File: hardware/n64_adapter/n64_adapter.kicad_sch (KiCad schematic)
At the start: 7 parts, among them J1 N64_Slot, J2 CART SLOT TOP ROW, J3 CART SLOT BOTTOM ROW, J4 Conn_01x01, J5 Conn_01x01, J6 Conn_01x01

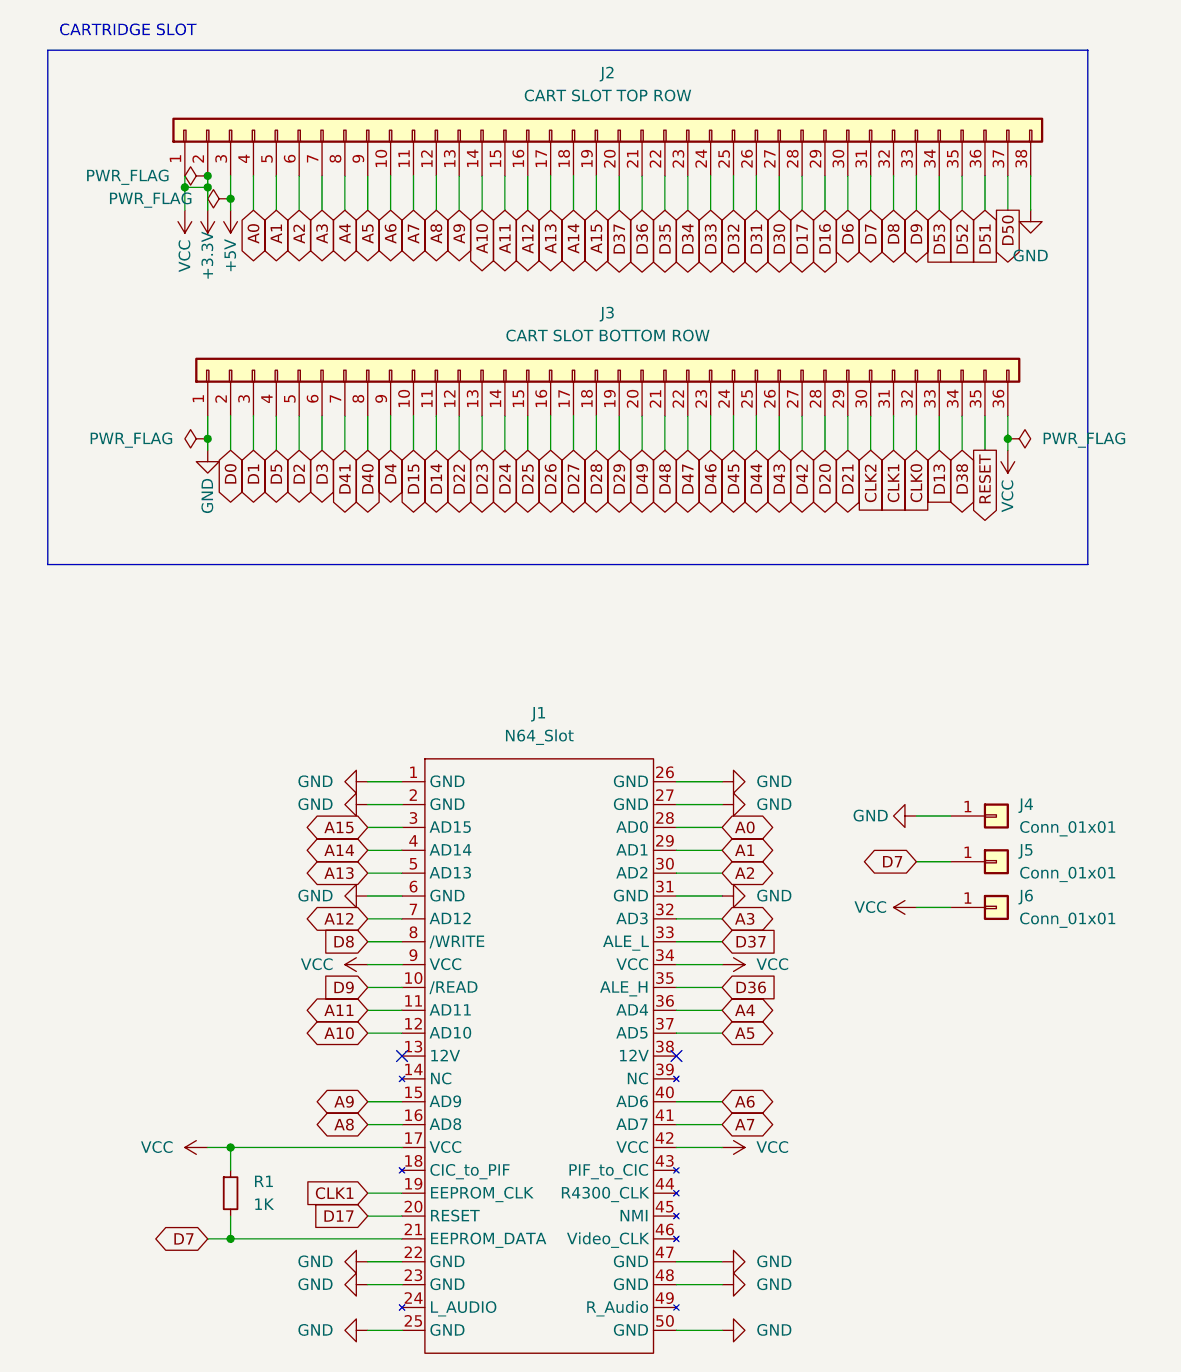
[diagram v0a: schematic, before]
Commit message: Update N64 breakout
add controller port to schematic and board. change board to inch standard, minimize trace width and reroute all traces. realign bottom silkscreen to pins.
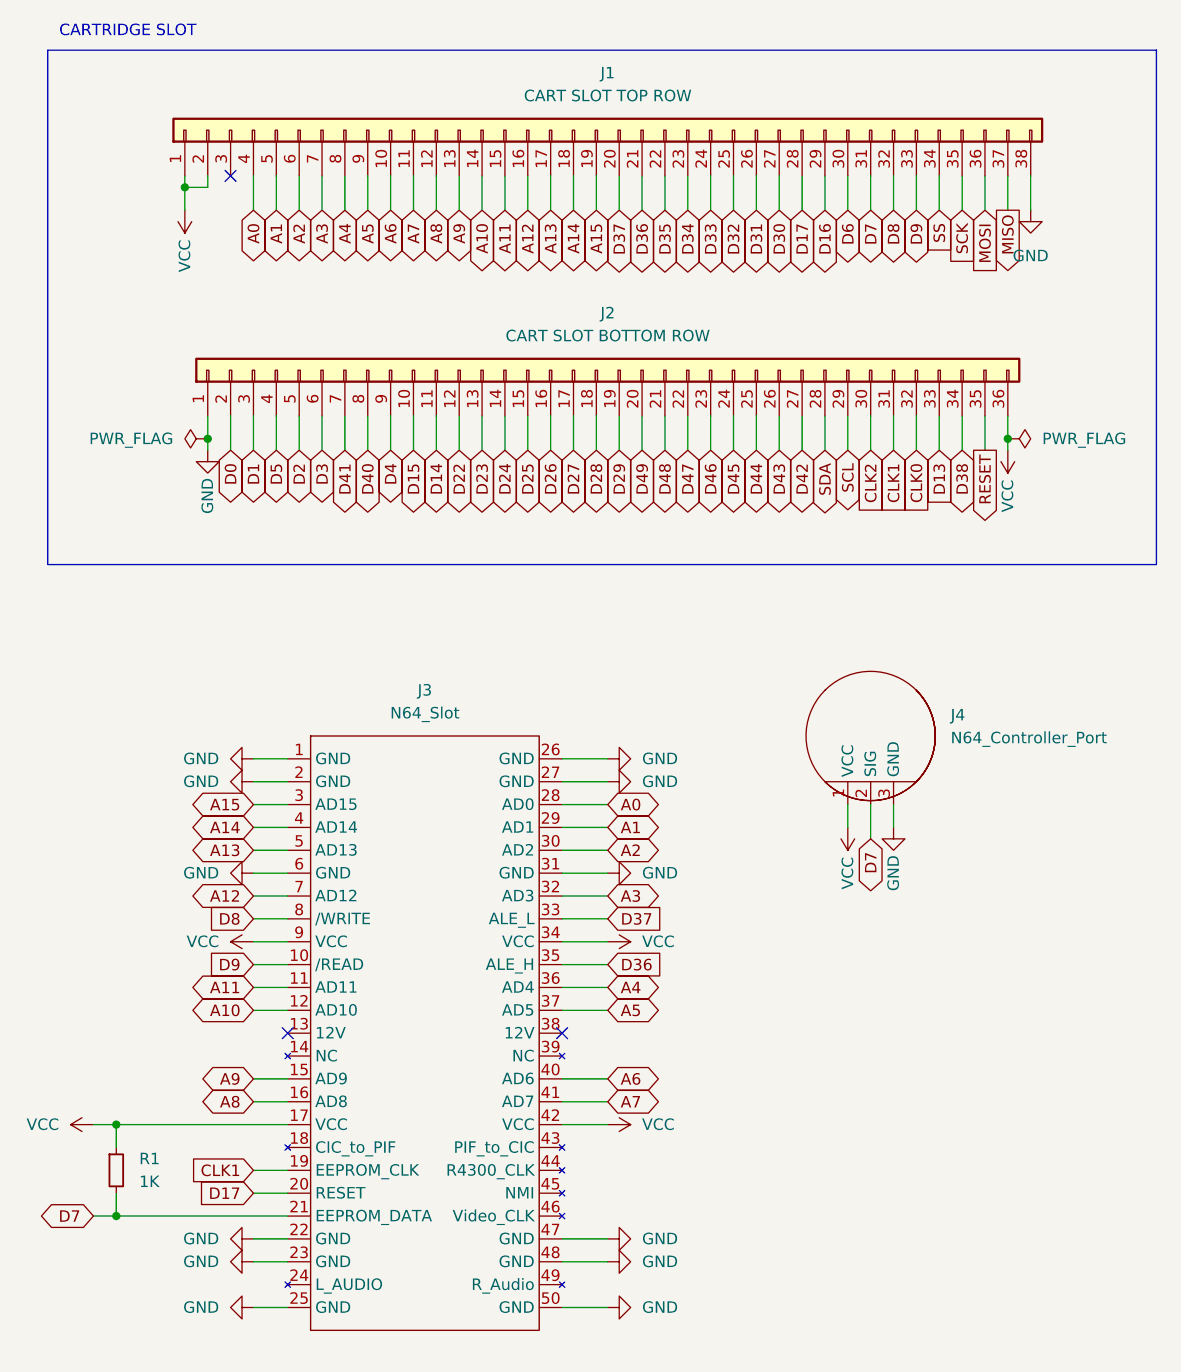
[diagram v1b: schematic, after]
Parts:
- removed J4, J5, J6: Conn_01x01, symbol Connector_Generic:Conn_01x01
- added J4: N64_Controller_Port, !OSCR:N64_CONTROLLER_PORT, symbol !OSCR:N64_Controller_Port
- J1: renamed from J2; footprint Connector_PinSocket_2.54mm:PinSocket_1x38_P2.54mm_Vertical -> Connector_PinHeader_2.54mm:PinHeader_1x38_P2.54mm_Vertical
- J2: renamed from J3; footprint Connector_PinSocket_2.54mm:PinSocket_1x36_P2.54mm_Vertical -> Connector_PinHeader_2.54mm:PinHeader_1x36_P2.54mm_Vertical
- J3: renamed from J1; footprint (none) -> !OSCR:N64 Slot; symbol sanni:N64_Slot -> !OSCR:N64_Slot
- R1: footprint (none) -> Resistor_THT:R_Axial_DIN0207_L6.3mm_D2.5mm_P10.16mm_Horizontal
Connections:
- net D7: now also J4.2 (SIG)
- net GND: now also J4.3 (GND)
- net +3V3 renamed VCC
- net VCC: now also J4.1 (VCC)
- net +5V: no longer names the net of J1.3 (Pin_3)
- net D20 renamed SDA
- net D21 renamed SCL
- net D50 renamed MISO
- net D51 renamed MOSI
- net D52 renamed SCK
- net D53 renamed SS
- no-connect marks 2 -> 3
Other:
- title: OSCR N64 ADAPTER -> OSCR N64 Breakout
- moved on the sheet: J3, R1

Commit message: finalize n64 breakout design
Ready for RTM
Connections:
- net CLK0: no longer names the net of J2.32 (Pin_32)
- net CLK2: no longer names the net of J2.30 (Pin_30)
- net D0: no longer names the net of J2.2 (Pin_2)
- net D1: no longer names the net of J2.3 (Pin_3)
- net D13: no longer names the net of J2.33 (Pin_33)
- net D14: no longer names the net of J2.11 (Pin_11)
- net D15: no longer names the net of J2.10 (Pin_10)
- net D16: no longer names the net of J1.29 (Pin_29)
- net D2: no longer names the net of J2.5 (Pin_5)
- net D22: no longer names the net of J2.12 (Pin_12)
- net D23: no longer names the net of J2.13 (Pin_13)
- net D24: no longer names the net of J2.14 (Pin_14)
- net D25: no longer names the net of J2.15 (Pin_15)
- net D26: no longer names the net of J2.16 (Pin_16)
- net D27: no longer names the net of J2.17 (Pin_17)
- net D28: no longer names the net of J2.18 (Pin_18)
- net D29: no longer names the net of J2.19 (Pin_19)
- net D3: no longer names the net of J2.6 (Pin_6)
- net D30: no longer names the net of J1.27 (Pin_27)
- net D31: no longer names the net of J1.26 (Pin_26)
- net D32: no longer names the net of J1.25 (Pin_25)
- net D33: no longer names the net of J1.24 (Pin_24)
- net D34: no longer names the net of J1.23 (Pin_23)
- net D35: no longer names the net of J1.22 (Pin_22)
- net D38: no longer names the net of J2.34 (Pin_34)
- net D4: no longer names the net of J2.9 (Pin_9)
- net D40: no longer names the net of J2.8 (Pin_8)
- net D41: no longer names the net of J2.7 (Pin_7)
- net D42: no longer names the net of J2.27 (Pin_27)
- net D43: no longer names the net of J2.26 (Pin_26)
- net D44: no longer names the net of J2.25 (Pin_25)
- net D45: no longer names the net of J2.24 (Pin_24)
- net D46: no longer names the net of J2.23 (Pin_23)
- net D47: no longer names the net of J2.22 (Pin_22)
- net D48: no longer names the net of J2.21 (Pin_21)
- net D49: no longer names the net of J2.20 (Pin_20)
- net D5: no longer names the net of J2.4 (Pin_4)
- net D6: no longer names the net of J1.30 (Pin_30)
- net MISO: no longer names the net of J1.37 (Pin_37)
- net MOSI: no longer names the net of J1.36 (Pin_36)
- net RESET: no longer names the net of J2.35 (Pin_35)
- net SCK: no longer names the net of J1.35 (Pin_35)
- net SCL: no longer names the net of J2.29 (Pin_29)
- net SDA: no longer names the net of J2.28 (Pin_28)
- net SS: no longer names the net of J1.34 (Pin_34)
- no-connect marks 3 -> 48
